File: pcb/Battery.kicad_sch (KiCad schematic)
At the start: 32 parts, among them IC5 BQ28Z620DRZR, Q2 CSD16327Q3, Q3 CSD16327Q3, U3 1043, U4 1043

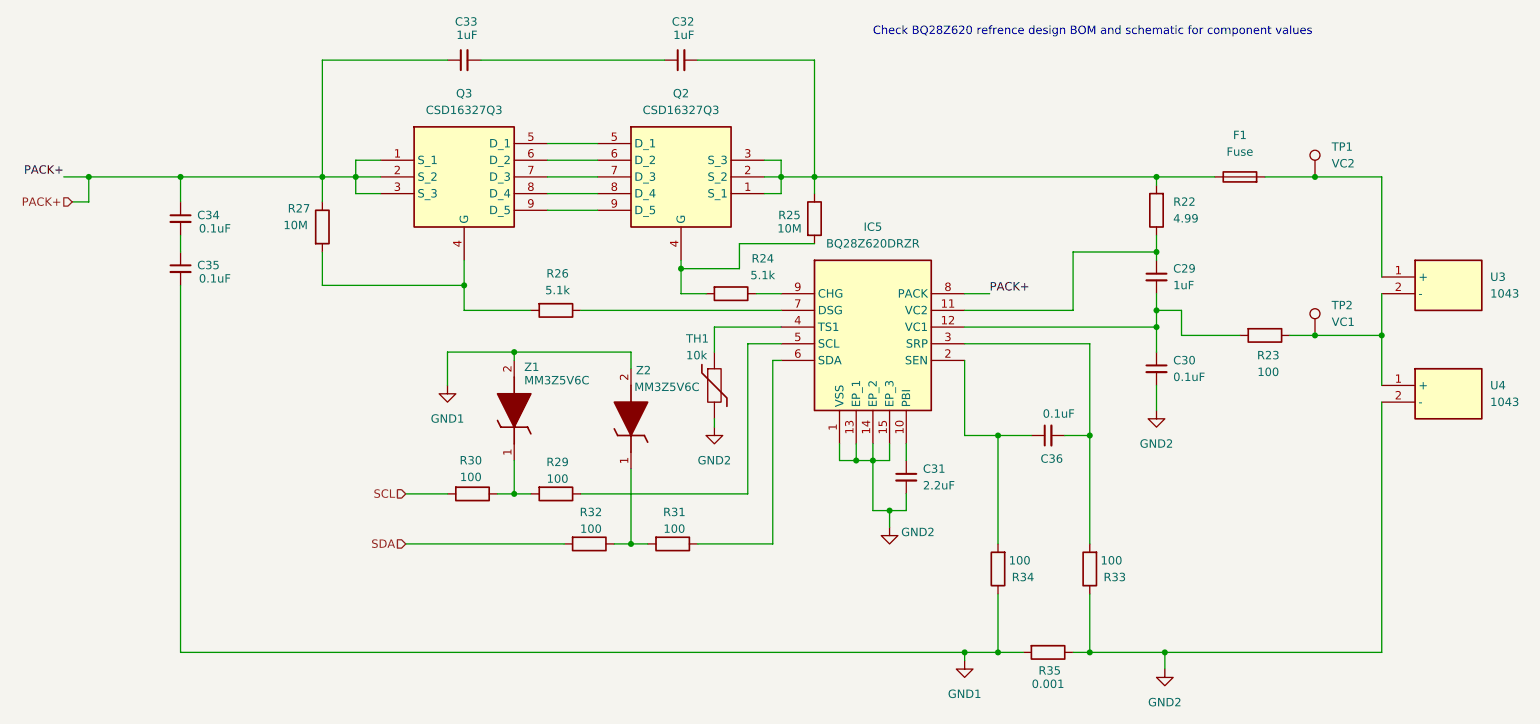
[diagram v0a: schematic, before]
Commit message: latest updates to schematic, changed to continuous ground
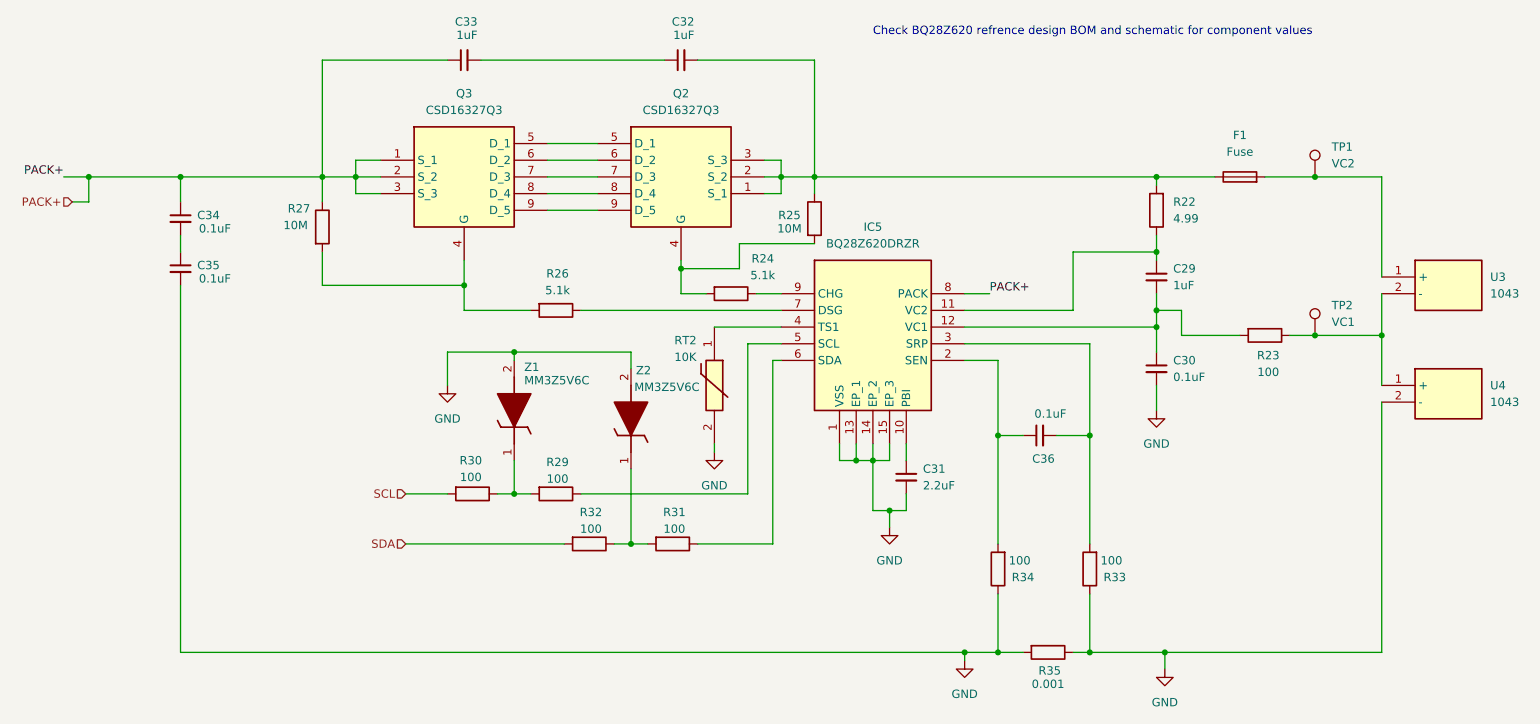
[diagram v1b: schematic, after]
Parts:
- removed TH1: 10k, symbol Device:Thermistor
- added RT2: 10K, 103AT-2:103AT2, symbol 103AT-2:103AT-2
- C29, C30, C31, C32, C33, C34, C35, C36: footprint (none) -> Capacitor_SMD:C_0805_2012Metric
- F1: footprint (none) -> Fuse:Fuse_0805_2012Metric
- IC5: footprint BQ28Z610DRZT -> BQ28Z620DRZR:BQ28Z610DRZT
- Q2, Q3: footprint CSD16327Q3 -> CSD16327Q3:CSD16327Q3
- R22, R23, R24, R25, R26, R27, R29, R30, R31, R32, R33, R34, R35: footprint (none) -> Resistor_SMD:R_0805_2012Metric
- TP1, TP2: footprint (none) -> TestPoint:TestPoint_Pad_3.0x3.0mm
- U3, U4: footprint 1043 -> 1049P:1049
- Z1, Z2: footprint SODFL2513X100N -> MM3Z5V6C:SODFL2513X100N
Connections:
- net GND2 is gone; now on net GND: C30.2, C31.2, IC5.1 (VSS), IC5.13 (EP_1), IC5.14 (EP_2), IC5.15 (EP_3), R33.1, R35.1, U4.2 (-)
- net at IC5.4 (TS1): now also RT2.1
- net GND1 renamed GND
- net GND: now also RT2.2
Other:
- moved on the sheet: C36
